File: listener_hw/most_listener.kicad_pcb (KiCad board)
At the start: 2 copper layers, 130 x 90 mm, 155 parts, among them J1 1-1394640-1, J2 ANALYSER, J3 I2S, J4 VBAT_IN, J5 PLR135/T10, J6 PLT133/T10W, J7 RCA 75R, J8 LINE L, J9 LINE R, M1 Tang Nano 20K, M2 ESP32-DevKitC-VIE, U1 74LVC1G34, U10 TPS2553DBVR, U11 74LVC1G123, U12 DIR9001, U13 SRC4192, U14 LP5907MFX-3.3, U15 PCM5102A, U16 LP5907MFX-3.3, U2 74LVC1G157, U3 74LVC1G125, U4 74LVC1G123, U5 TPS7B8133DRV, U6 LMR38020F, U7 Si514, U8 LP5907MFX-3.3, U9 74LVC1G79, X1 24.576MHz

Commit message: Board: narrowed to 123 x 90 mm; TP2 (TX_REGEN) and TP5 (RT_CLK) removed
The user asked for the board to be narrowed and for the probe points on
TX_REGEN and RT_CLK to go: no extra stubs on the regenerator's output into
the ring and on the Si514's clock into U9. Both come out of the sheet
(block 10's note says where the two can still be probed: U9's pins, M1's
TX_FB pin) and off the board; the signal points above J1 now are RX_BUF,
TX_SEL and WAKE, each beside a ground point.

Narrowing: the user had moved H5, J3 and J2 into the free strip right of M2.
Everything else right of the strip - block 9, the coax divider and J7, the
line-out block, the jacks on the right edge, the corner holes - moved 6.75 mm
left, the right edge and both ground pours with it; the jacks stay flush
with the new edge. ERC clean; DRC: no error, no difference from the sheet.

Co-Authored-By: Claude Opus 5.5 <noreply@anthropic.com>
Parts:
- removed TP2: TX_REGEN, TestPoint:TestPoint_Pad_D2.0mm
- removed TP5: RT_CLK, TestPoint:TestPoint_Pad_D2.0mm
- moved TP7 13.6 mm to (41.4, 62.5)
- moved TP3 13.4 mm to (15.0, 11.0)
- moved TP9 11.9 mm to (51.1, 62.5)
- moved H5 10.4 mm to (89.9, 4.32)
- moved J3 9.20 mm to (93.0, 55.6)
- moved J2 8.42 mm to (100.3, 55.9)
- moved C27 6.75 mm to (110.0, 26.4)
- moved C28 6.75 mm to (108.2, 23.3)
- moved C29 6.75 mm to (105.8, 40.6)
- moved C30 6.75 mm to (118.0, 20.2)
- moved C31 6.75 mm to (121.2, 20.2)
- moved C32 6.75 mm to (98.2, 18.3)
- moved C33 6.75 mm to (102.0, 15.2)
- moved C34 6.75 mm to (108.2, 19.9)
- moved C35 6.75 mm to (111.8, 19.9)
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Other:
- board size 130 x 90 mm -> 123.2 x 90 mm

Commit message: Board: 123 x 85 mm - the bottom edge up to the lowest part, the six M3 holes 4 mm from their edges
The user moved the battery input (F1, D2, D1, L2, C44, C45, C47) into the
empty bottom middle, U16 and C51 beside it, TP1 and TP4 elsewhere, M2 up a
little, and the two lower holes up, then asked for the height to shrink and
the M3 holes to be made uniform.

The bottom edge now sits 0.3 mm below the lowest courtyard (C47): the board
is 84.65 mm high instead of 90. Every hole is 4.0 mm from the edge it sits
at, as H1 and H2 always were: H3 and H4 at 4.0 mm above the new bottom edge
(H4 stays left of J8, where the user put it), H5 4.0 mm below the top, H6
and H3 4.0 mm in from the left. The ground pours follow the outline; the
antenna keep-out follows M2 again. DRC: no error, no difference from the
sheet.

Co-Authored-By: Claude Opus 5.5 <noreply@anthropic.com>
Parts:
- moved TP4 46.2 mm to (13.5, 62.0)
- moved C44 39.4 mm to (65.8, 66.0)
- moved D1 38.4 mm to (48.3, 79.8), turned to 180 degrees
- moved L2 36.9 mm to (53.1, 72.6)
- moved D2 36.1 mm to (41.1, 77.9)
- moved C45 21.8 mm to (65.9, 78.7)
- moved F1 20.6 mm to (30.4, 79.8), turned to 0 degrees
- moved H4 17.7 mm to (102.6, 80.7)
- moved C47 16.4 mm to (56.6, 82.8), turned to -90 degrees
- moved TP1 13.4 mm to (15.0, 17.0)
- moved U16 12.0 mm to (84.1, 77.7)
- moved H3 5.35 mm to (4.00, 80.7)
- moved C51 2.86 mm to (82.5, 66.8)
- moved M2 0.85 mm to (71.3, 26.1)
- moved H5 0.32 mm to (89.9, 4.00)
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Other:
- board size 123.2 x 90 mm -> 123.2 x 84.7 mm

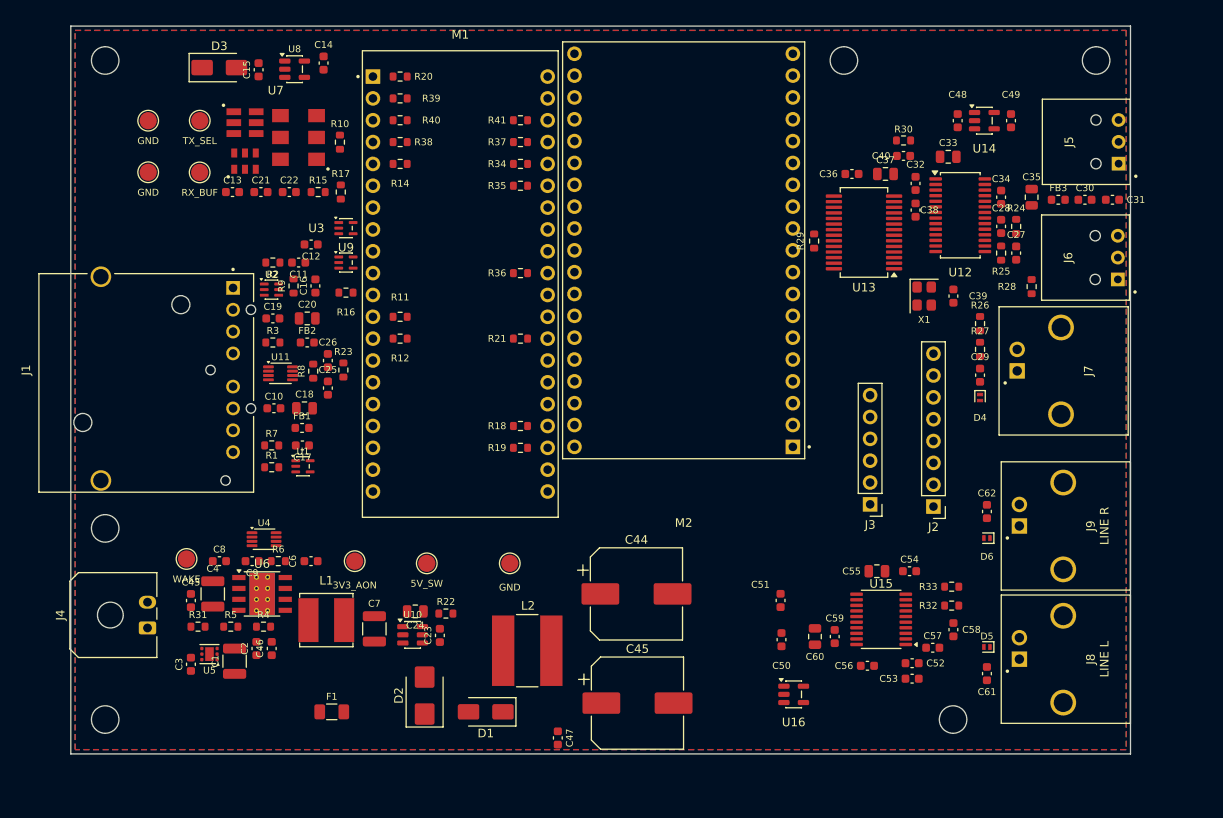
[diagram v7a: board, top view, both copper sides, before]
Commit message: Board: 125 x 80 mm - 1 mm off the top, the bottom up to 80 mm, the right edge 1.75 mm out
Asked for by the user: C44/C45 and the lower holes up so the board is
125 x 80 mm, with 1 mm off the top and the rest off the bottom.

- Top: the outline starts 1 mm lower and the whole board moved up by that
  1 mm, so the top holes H1, H2, H5 stay 4.0 mm from the edge. M2's USB
  socket now reaches 0.65 mm past the top edge, as a socket at the edge should.
- Bottom: the new edge is 80 mm down. C44 and C45 moved up 3.6 mm together,
  C47 beside C45; F1, D1, D2 and L2 up by 0.45 to 1.3 mm; J8 and J9 up
  1 mm with D6/C62; J4 up 0.5 mm to clear H3; C53 and C61 moved to clear
  H4. H3 and H4 sit 4.0 mm above the new bottom edge.
- Width: the right edge 1.75 mm further out; the five jacks, their edge-side
  parts (FB3, C30, C31, R28, the coax divider and D4, D5/C61, D6/C62) and H2
  followed it, the jacks flush with the edge as before.

The ground pours follow the outline, the antenna keep-out follows M2. DRC:
no error, no difference from the sheet; the warnings are silk.

Co-Authored-By: Claude Opus 5.5 <noreply@anthropic.com>
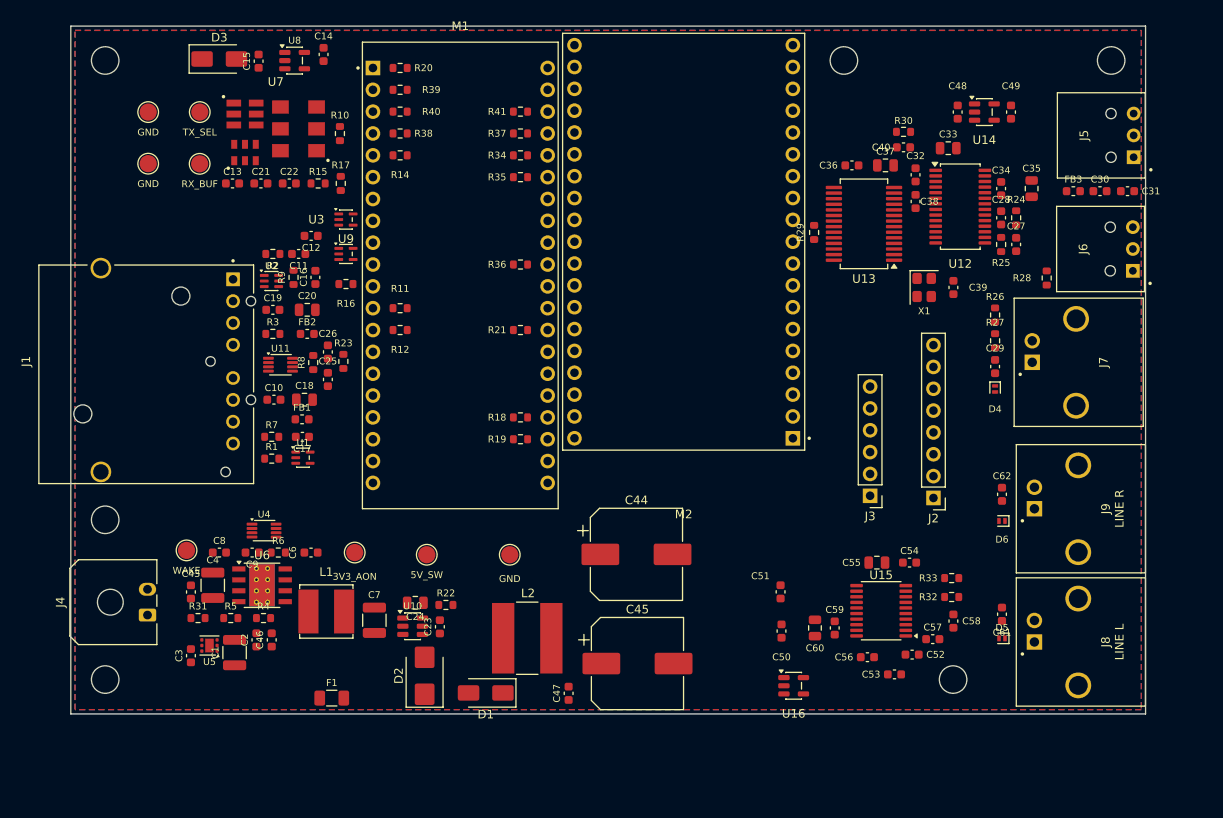
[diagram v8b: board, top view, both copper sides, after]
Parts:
- moved C61 7.13 mm to (108.3, 68.4)
- moved C47 5.34 mm to (57.9, 77.6), turned to 90 degrees
- moved H3 4.65 mm to (4.00, 76.0)
- moved H4 4.65 mm to (102.6, 76.0)
- moved C44 4.60 mm to (65.8, 61.4)
- moved C45 4.60 mm to (65.9, 74.1)
- moved C62 2.66 mm to (108.3, 54.5)
- moved D6 2.66 mm to (108.3, 57.6)
- moved J8 2.66 mm to (112.1, 71.6)
- moved J9 2.66 mm to (112.1, 56.1)
- moved D2 2.30 mm to (41.1, 75.6)
- moved D1 2.20 mm to (48.3, 77.6)
- moved C53 2.11 mm to (95.8, 75.4)
- moved C29 2.02 mm to (107.5, 39.6)
- moved C30 2.02 mm to (119.7, 19.2)
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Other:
- board size 123.2 x 84.7 mm -> 125 x 80 mm
